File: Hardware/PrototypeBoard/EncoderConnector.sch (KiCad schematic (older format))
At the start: 9 parts

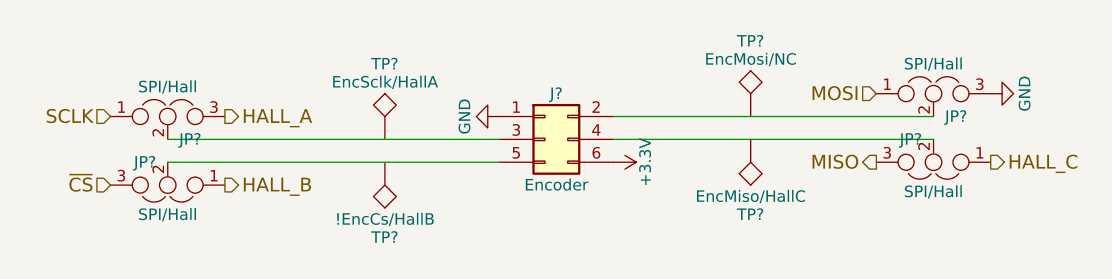
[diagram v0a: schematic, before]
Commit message: Fixed all ERC errors. Added power consumption estimation and other comments. Added links to datasheets. Dimensioned low pass and voltage dividers. Added TVS diodes for protection of voltage rails and ADC inputs. Added fuses. Added Testpoints. Added DC-link capacitors.
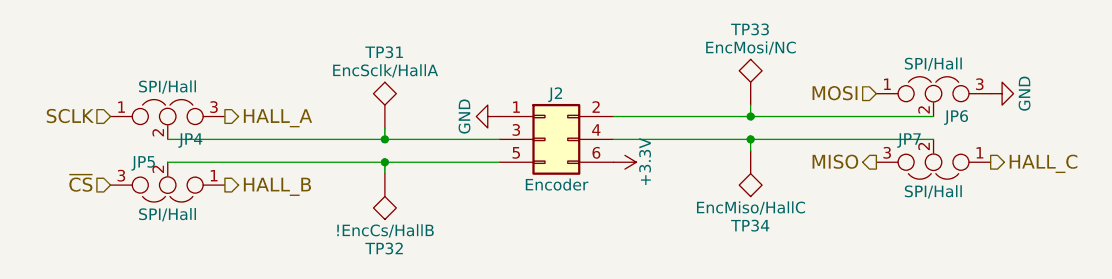
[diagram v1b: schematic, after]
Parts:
- gave numbers to parts that had none: 9
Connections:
- net at J2.2 (Pin_2), JP6.2: now also TP33.1
- net at J2.3 (Pin_3), JP4.2: now also TP31.1
- net at J2.4 (Pin_4), JP7.2: now also TP34.1
- net at J2.5 (Pin_5), JP5.2: now also TP32.1
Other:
- moved on the sheet: TP31, TP32, TP33, TP34
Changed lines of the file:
@@
 $EndDescr
 $Comp
-L Conn_02x03_Odd_Even J?
+L Conn_02x03_Odd_Even J2
 U 1 1 5AFC940D
 P 6000 2350
-F 0 "J?" H 6050 2550 50  0000 C CNN
+F 0 "J2" H 6050 2550 50  0000 C CNN
 F 1 "Encoder" H 6050 2150 50  0000 C CNN
 F 2 "" H 6000 2350 50  0001 C CNN
@@
 $EndComp
 $Comp
-L GND #PWR?
+L GND #PWR064
 U 1 1 5AFC9462
 P 5800 2250
-F 0 "#PWR?" H 5800 2000 50  0001 C CNN
+F 0 "#PWR064" H 5800 2000 50  0001 C CNN
 F 1 "GND" H 5800 2100 50  0000 C CNN
 F 2 "" H 5800 2250 50  0001 C CNN
@@
 $EndComp
 $Comp
-L +3.3V #PWR?
+L +3.3V #PWR065
 U 1 1 5AFC948F
 P 6300 2450
-F 0 "#PWR?" H 6300 2300 50  0001 C CNN
+F 0 "#PWR065" H 6300 2300 50  0001 C CNN
 F 1 "+3.3V" H 6300 2590 50  0000 C CNN
 F 2 "" H 6300 2450 50  0001 C CNN
@@
 HALL_B
 $Comp
-L Jumper_NC_Dual JP?
+L Jumper_NC_Dual JP4
 U 1 1 5AFC952B
 P 4350 2250
-F 0 "JP?" H 4400 2150 50  0000 L CNN
+F 0 "JP4" H 4400 2150 50  0000 L CNN
 F 1 "SPI/Hall" H 4350 2350 50  0000 C BNN
 F 2 "" H 4350 2250 50  0001 C CNN
@@
 $EndComp
 $Comp
-L Jumper_NC_Dual JP?
+L Jumper_NC_Dual JP5
 U 1 1 5AFC9571
 P 4350 2550
-F 0 "JP?" H 4400 2450 50  0000 L CNN
+F 0 "JP5" H 4400 2450 50  0000 L CNN
 F 1 "SPI/Hall" H 4350 2650 50  0000 C BNN
 F 2 "" H 4350 2550 50  0001 C CNN
@@
 $EndComp
 $Comp
-L Jumper_NC_Dual JP?
+L Jumper_NC_Dual JP6
 U 1 1 5AFC95E5
 P 7700 2150
-F 0 "JP?" H 7750 2050 50  0000 L CNN
+F 0 "JP6" H 7750 2050 50  0000 L CNN
 F 1 "SPI/Hall" H 7700 2250 50  0000 C BNN
 F 2 "" H 7700 2150 50  0001 C CNN
@@
 $EndComp
 $Comp
-L Jumper_NC_Dual JP?
+L Jumper_NC_Dual JP7
 U 1 1 5AFC9628
 P 7700 2450
-F 0 "JP?" H 7750 2350 50  0000 L CNN
+F 0 "JP7" H 7750 2350 50  0000 L CNN
 F 1 "SPI/Hall" H 7700 2550 50  0000 C BNN
 F 2 "" H 7700 2450 50  0001 C CNN
@@
 	6300 2250 7700 2250
 $Comp
-L GND #PWR?
+L GND #PWR066
 U 1 1 5AFC9686
 P 7950 2150
-F 0 "#PWR?" H 7950 1900 50  0001 C CNN
+F 0 "#PWR066" H 7950 1900 50  0001 C CNN
 F 1 "GND" H 7950 2000 50  0000 C CNN
 F 2 "" H 7950 2150 50  0001 C CNN
@@
 HALL_C
 $Comp
-L TEST TP?
+L TEST TP31
 U 1 1 5AFF16A3
-P 5300 2350
-F 0 "TP?" H 5300 2650 50  0000 C BNN
-F 1 "EncSclk/HallA" H 5300 2600 50  0000 C CNN
-F 2 "" H 5300 2350 50  0001 C CNN
-F 3 "" H 5300 2350 50  0001 C CNN
-	1    5300 2350
+P 5300 2300
+F 0 "TP31" H 5300 2600 50  0000 C BNN
+F 1 "EncSclk/HallA" H 5300 2550 50  0000 C CNN
+F 2 "" H 5300 2300 50  0001 C CNN
+F 3 "" H 5300 2300 50  0001 C CNN
+	1    5300 2300
 	1    0    0    -1
 $EndComp
 $Comp
-L TEST TP?
+L TEST TP32
 U 1 1 5AFF1700
-P 5300 2450
-F 0 "TP?" H 5300 2750 50  0000 C BNN
-F 1 "!EncCs/HallB" H 5300 2700 50  0000 C CNN
-F 2 "" H 5300 2450 50  0001 C CNN
-F 3 "" H 5300 2450 50  0001 C CNN
-	1    5300 2450
+P 5300 2500
+F 0 "TP32" H 5300 2800 50  0000 C BNN
+F 1 "!EncCs/HallB" H 5300 2750 50  0000 C CNN
+F 2 "" H 5300 2500 50  0001 C CNN
+F 3 "" H 5300 2500 50  0001 C CNN
+	1    5300 2500
 	-1   0    0    1
 $EndComp
 $Comp
-L TEST TP?
+L TEST TP34
 U 1 1 5AFF1757
-P 6900 2350
-F 0 "TP?" H 6900 2650 50  0000 C BNN
-F 1 "EncMiso/HallC" H 6900 2600 50  0000 C CNN
-F 2 "" H 6900 2350 50  0001 C CNN
-F 3 "" H 6900 2350 50  0001 C CNN
-	1    6900 2350
+P 6900 2400
+F 0 "TP34" H 6900 2700 50  0000 C BNN
+F 1 "EncMiso/HallC" H 6900 2650 50  0000 C CNN
+F 2 "" H 6900 2400 50  0001 C CNN
+F 3 "" H 6900 2400 50  0001 C CNN
+	1    6900 2400
 	-1   0    0    1
 $EndComp
 $Comp
-L TEST TP?
+L TEST TP33
 U 1 1 5AFF17C5
-P 6900 2250
-F 0 "TP?" H 6900 2550 50  0000 C BNN
-F 1 "EncMosi/NC" H 6900 2500 50  0000 C CNN
-F 2 "" H 6900 2250 50  0001 C CNN
-F 3 "" H 6900 2250 50  0001 C CNN
-	1    6900 2250
+P 6900 2200
+F 0 "TP33" H 6900 2500 50  0000 C BNN
+F 1 "EncMosi/NC" H 6900 2450 50  0000 C CNN
+F 2 "" H 6900 2200 50  0001 C CNN
+F 3 "" H 6900 2200 50  0001 C CNN
+	1    6900 2200
 	1    0    0    -1
 $EndComp
+Wire Wire Line
+	5300 2300 5300 2350
+Connection ~ 5300 2350
+Wire Wire Line
+	5300 2500 5300 2450
+Connection ~ 5300 2450
+Wire Wire Line
+	6900 2400 6900 2350
+Connection ~ 6900 2350
+Wire Wire Line
+	6900 2200 6900 2250
+Connection ~ 6900 2250
 $EndSCHEMATC

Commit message: forgot files
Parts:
- J2: footprint (none) -> Pin_Headers:Pin_Header_Straight_1x06_Pitch2.54mm
- JP4, JP5, JP6, JP7: footprint (none) -> Connectors:PINHEAD1-3
- TP31, TP32, TP33, TP34: footprint (none) -> Measurement_Points:Measurement_Point_Round-TH_Big
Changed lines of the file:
@@
 F 0 "J2" H 6050 2550 50  0000 C CNN
 F 1 "Encoder" H 6050 2150 50  0000 C CNN
-F 2 "" H 6000 2350 50  0001 C CNN
+F 2 "Pin_Headers:Pin_Header_Straight_1x06_Pitch2.54mm" H 6000 2350 50  0001 C CNN
 F 3 "" H 6000 2350 50  0001 C CNN
 	1    6000 2350
@@
 F 0 "JP4" H 4400 2150 50  0000 L CNN
 F 1 "SPI/Hall" H 4350 2350 50  0000 C BNN
-F 2 "" H 4350 2250 50  0001 C CNN
+F 2 "Connectors:PINHEAD1-3" H 4350 2250 50  0001 C CNN
 F 3 "" H 4350 2250 50  0001 C CNN
 	1    4350 2250
@@
 F 0 "JP5" H 4400 2450 50  0000 L CNN
 F 1 "SPI/Hall" H 4350 2650 50  0000 C BNN
-F 2 "" H 4350 2550 50  0001 C CNN
+F 2 "Connectors:PINHEAD1-3" H 4350 2550 50  0001 C CNN
 F 3 "" H 4350 2550 50  0001 C CNN
 	1    4350 2550
@@
 F 0 "JP6" H 7750 2050 50  0000 L CNN
 F 1 "SPI/Hall" H 7700 2250 50  0000 C BNN
-F 2 "" H 7700 2150 50  0001 C CNN
+F 2 "Connectors:PINHEAD1-3" H 7700 2150 50  0001 C CNN
 F 3 "" H 7700 2150 50  0001 C CNN
 	1    7700 2150
@@
 F 0 "JP7" H 7750 2350 50  0000 L CNN
 F 1 "SPI/Hall" H 7700 2550 50  0000 C BNN
-F 2 "" H 7700 2450 50  0001 C CNN
+F 2 "Connectors:PINHEAD1-3" H 7700 2450 50  0001 C CNN
 F 3 "" H 7700 2450 50  0001 C CNN
 	1    7700 2450
@@
 F 0 "TP31" H 5300 2600 50  0000 C BNN
 F 1 "EncSclk/HallA" H 5300 2550 50  0000 C CNN
-F 2 "" H 5300 2300 50  0001 C CNN
+F 2 "Measurement_Points:Measurement_Point_Round-TH_Big" H 5300 2300 50  0001 C CNN
 F 3 "" H 5300 2300 50  0001 C CNN
 	1    5300 2300
@@
 F 0 "TP32" H 5300 2800 50  0000 C BNN
 F 1 "!EncCs/HallB" H 5300 2750 50  0000 C CNN
-F 2 "" H 5300 2500 50  0001 C CNN
+F 2 "Measurement_Points:Measurement_Point_Round-TH_Big" H 5300 2500 50  0001 C CNN
 F 3 "" H 5300 2500 50  0001 C CNN
 	1    5300 2500
@@
 F 0 "TP34" H 6900 2700 50  0000 C BNN
 F 1 "EncMiso/HallC" H 6900 2650 50  0000 C CNN
-F 2 "" H 6900 2400 50  0001 C CNN
+F 2 "Measurement_Points:Measurement_Point_Round-TH_Big" H 6900 2400 50  0001 C CNN
 F 3 "" H 6900 2400 50  0001 C CNN
 	1    6900 2400
@@
 F 0 "TP33" H 6900 2500 50  0000 C BNN
 F 1 "EncMosi/NC" H 6900 2450 50  0000 C CNN
-F 2 "" H 6900 2200 50  0001 C CNN
+F 2 "Measurement_Points:Measurement_Point_Round-TH_Big" H 6900 2200 50  0001 C CNN
 F 3 "" H 6900 2200 50  0001 C CNN
 	1    6900 2200
